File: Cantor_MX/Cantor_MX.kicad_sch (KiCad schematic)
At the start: 23 parts, among them J1 TRRS, K00 KEYSW, K01 KEYSW, K02 KEYSW, K03 KEYSW, K04 KEYSW, K05 KEYSW, K10 KEYSW, K11 KEYSW, K12 KEYSW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

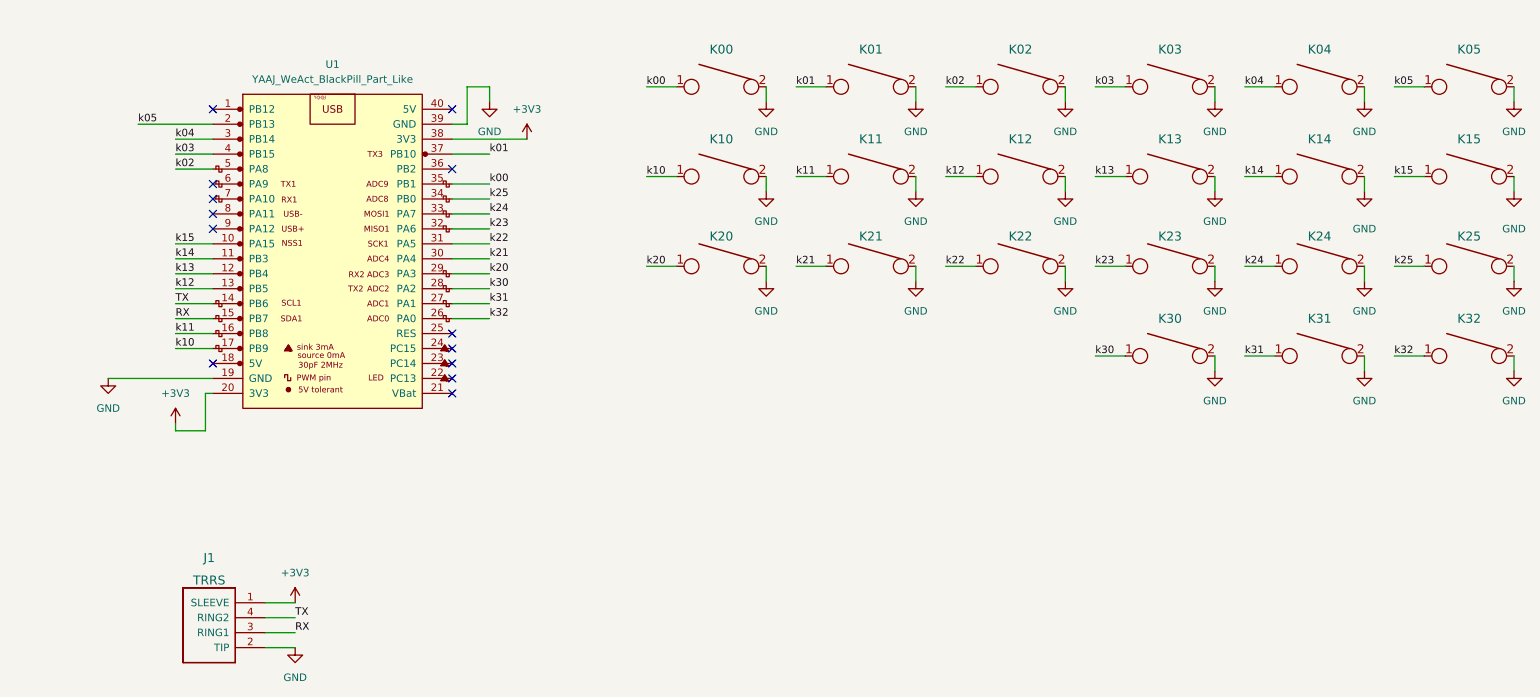
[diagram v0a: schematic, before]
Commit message: Dialed in teardrops Moved most horizontal traces under MCU to back Backside silk logo tweak Updated drawing sheets attributions and versions Regenerated Gerbers
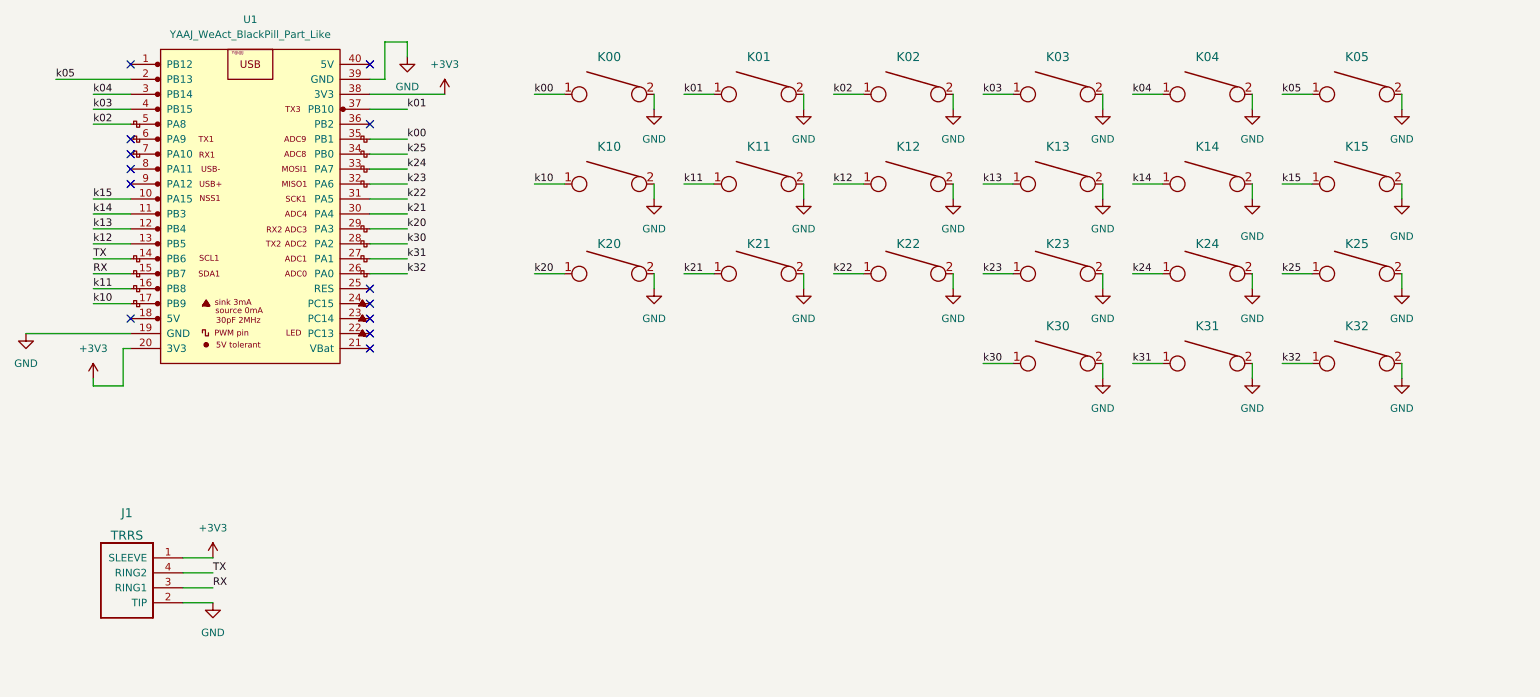
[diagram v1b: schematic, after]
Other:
- title: (none) -> Cantor MX
- moved on the sheet: J1, K00, K01, K02, K03, K04, K05, K10, K11, K12, K13, K14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
